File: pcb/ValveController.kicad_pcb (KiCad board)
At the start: 4 copper layers, 99 x 72 mm, 52 parts, among them J10 1770966, J11 1770966, J12 1770966, J13 USB4105-GF-A, J2 1990986, J3 1990986, J8 1770966, J9 1770966, Q3 MOC3063S-TA1, Q4 MOC3063S-TA1, SW1 TL9320AF400QG, U1 IRM-03-5, U2 TLV75733P, U5 ESP32-C6-WROOM-1-N4

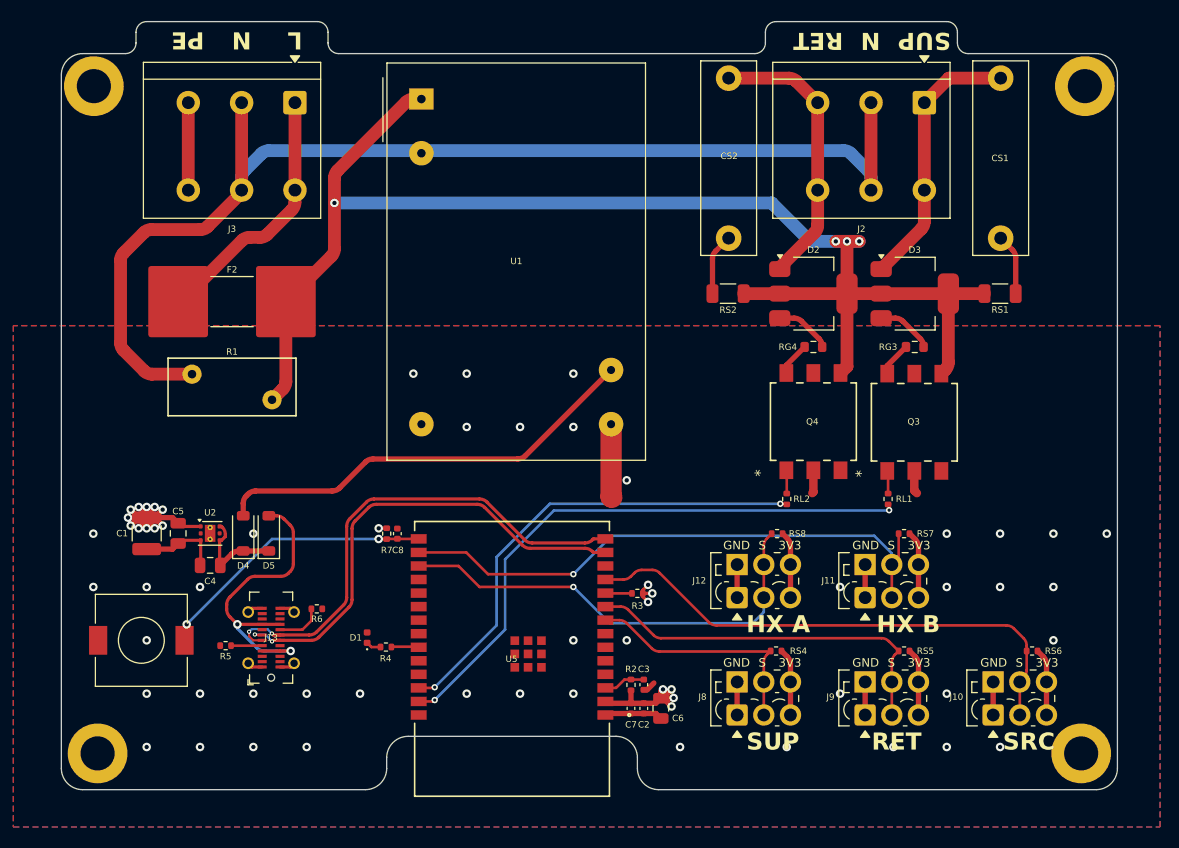
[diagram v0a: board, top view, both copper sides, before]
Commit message: chore(pcb): reorganize into pcb/ and consolidate 3D models
Move the KiCad project into pcb/, flatten custom STEP models into pcb/3dmodels/ (rewriting the KIPRJMOD-relative model paths in the board and footprints), relocate manual .bak snapshots to git-ignored pcb/backups/, and drop regenerable gerber outputs. Restore .gitignore.
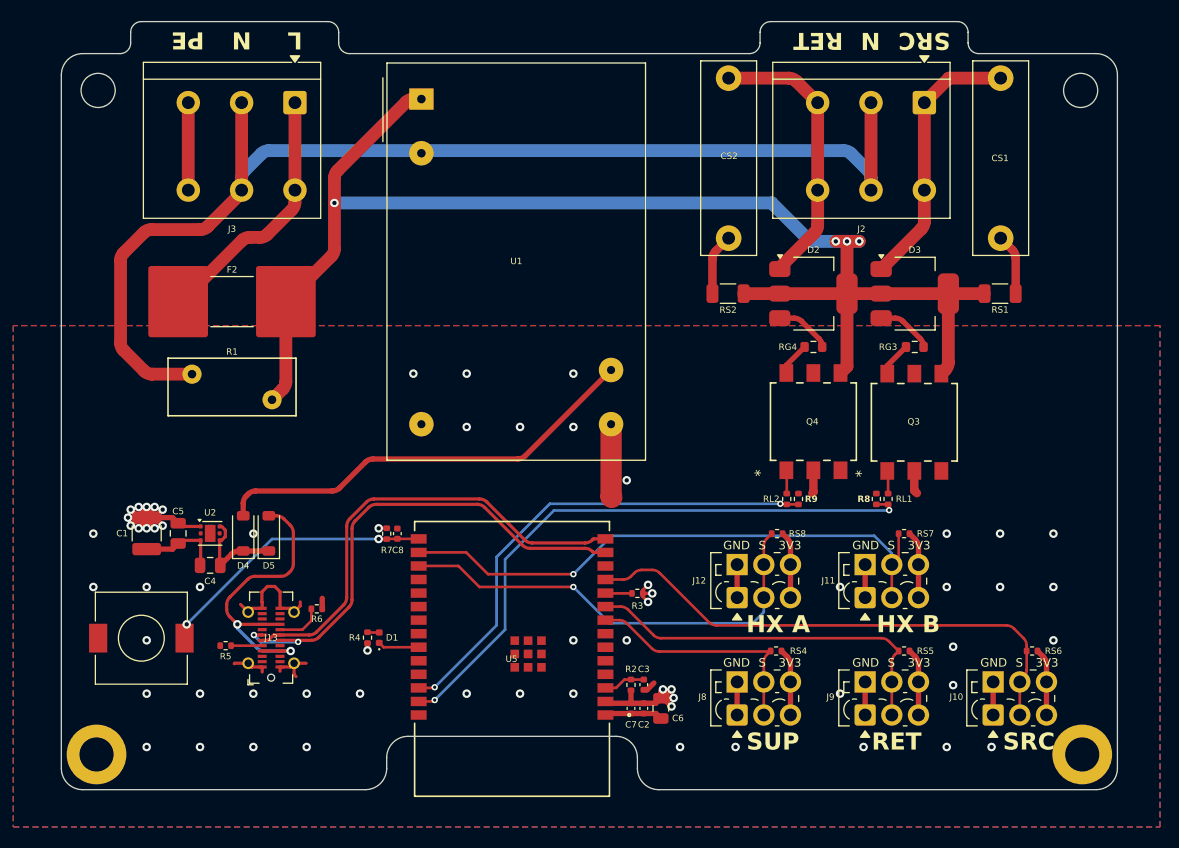
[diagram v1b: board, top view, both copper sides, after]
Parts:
- added R8: 10k, Resistor_SMD:R_0402_1005Metric, F.Cu at (138.4, 81.8)
- added R9: 10k, Resistor_SMD:R_0402_1005Metric, F.Cu at (131.1, 81.8)
- D1: value LED -> LED (active-low)
- H1, H2: footprint MountingHole:MountingHole_3.2mm_M3_DIN965_Pad -> MountingHole:MountingHole_3.2mm_M3_DIN965
- J13: value USB4105-GF-A -> USB4115-03-C
- moved R4 1.94 mm to (90.7, 94.8), turned to 90 degrees
- moved D1 1.13 mm to (91.8, 94.8)
- moved H1 0.57 mm to (65.5, 43.5)
- moved H2 0.57 mm to (157.6, 43.5)
- moved SW1 0.20 mm to (69.5, 94.8)
- moved H3 0.14 mm to (65.3, 105.7)
- moved H4 0.14 mm to (157.7, 105.7)
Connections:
- D1 pad 1: LED_A -> STAT_LED
- D1 pad 2: GND -> LED_A
- H3 pad 1: (no net) -> GND
- H4 pad 1: (no net) -> GND
- R4 pad 1: STAT_LED -> 3V3
- U5 pad 24: DBG_RX -> unconnected-(U5-RXD0-Pad24)
- U5 pad 25: DBG_TX -> unconnected-(U5-TXD0-Pad25)
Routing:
- net GND: track 47.0 -> 60.1 mm
- net USB_D+: track 46.7 -> 43.6 mm, vias 2 -> 0
- net USB_D-: track 45.1 -> 47.1 mm
- net STAT_LED: track 2.50 -> 3.87 mm
- net SSR_OPEN: track 56.0 -> 57.1 mm
- net SSR_CLOSE: track 45.4 -> 46.5 mm
- net 3V3: track 66.2 -> 66.9 mm, vias 19 -> 20
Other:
- outline, holes or cut-outs redrawn

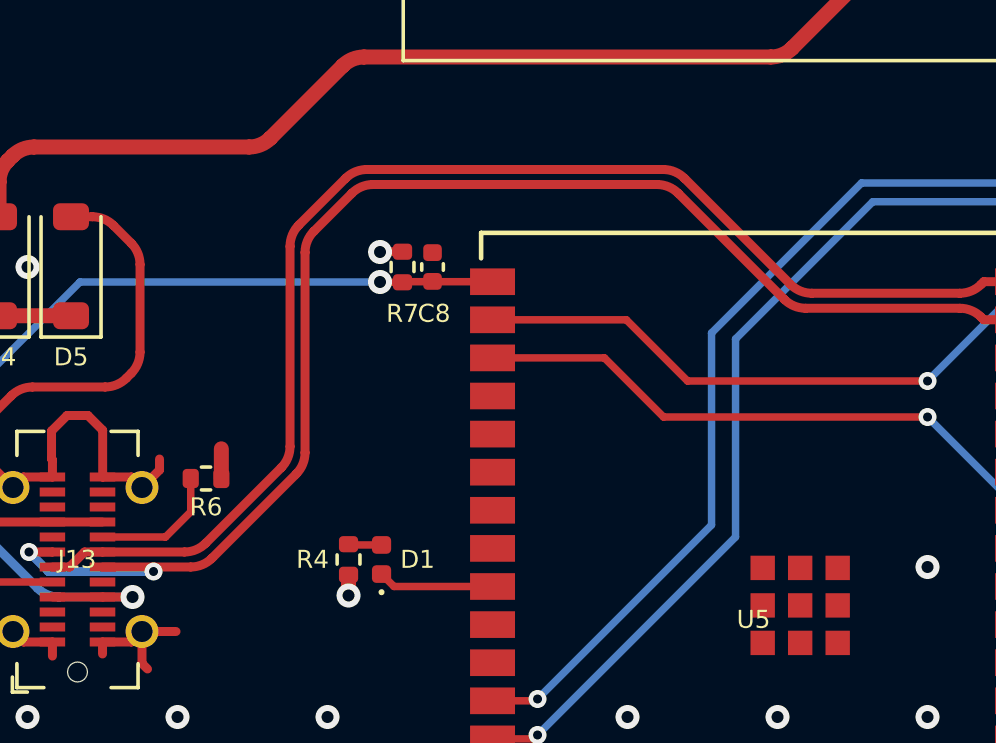
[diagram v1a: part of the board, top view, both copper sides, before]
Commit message: chore(pcb): add CUI UJ20 USB-C library and continue routing
Adds the CUI UJ20-C-V-C-3-SMT-TR vertical USB-C part (symbol, footprint
and STEP) as a project-local library, registered through a new
sym-lib-table plus an extra fp-lib-table entry. The board still places the
GCT USB4115-03-C on J13 — the UJ20 is available but not swapped in yet.

Also re-saves the PCB with incremental routing (405 -> 413 track/via
elements) and picks up a reordered used_designators list, now including J1.
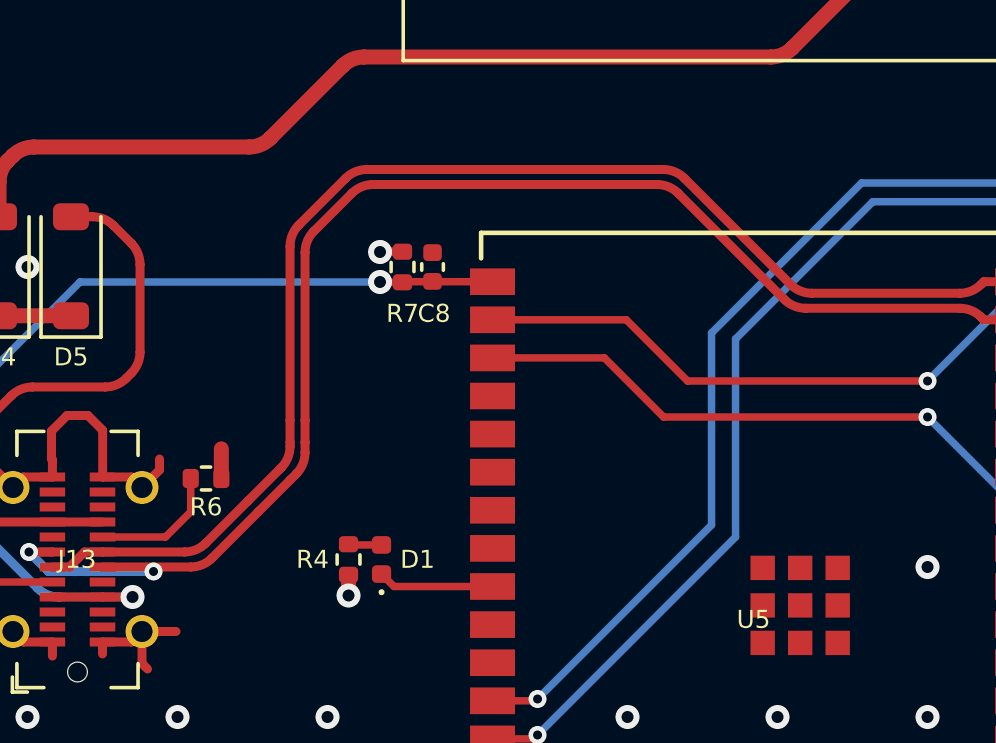
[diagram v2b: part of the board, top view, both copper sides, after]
